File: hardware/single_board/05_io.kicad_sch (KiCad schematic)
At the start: 36 parts, among them J12 USB-C, J13 EXPANSION, J14 RS485 IN, J15 RS485 OUT, SW1 BOOTSEL, U13 USBLC6-2SC6, U14 SIT3088ETK, U15 SIT3088ETK, U17 SIT3088ETK, U18 SIT3088ETK

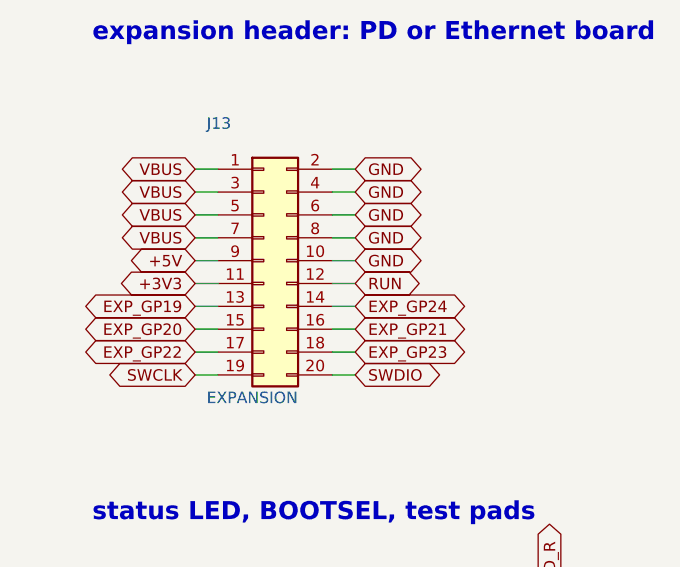
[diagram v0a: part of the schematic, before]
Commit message: Board S: screw keepouts, finer In3 centre rules, encoder on SPI0 (WIP, unrouted)
Work in progress from 2026-09-24/25, saved before routing is finished.
The board file here is the generator's output, not a routed board.

- Keepouts on F.Cu and B.Cu round the four centre motor screws
- USB-C placed tangent to the edge
- Encoder on SPI0 (ENC_DO GPIO4, ENC_SCK GPIO6); J13 pins swapped
- C901 moved north; encoder stitching vias back in the chip's pads
- "fine centre" rule area: signal nets on In3 inside R 17 may use
  0.12 mm track and clearance (servodrive_S.kicad_dru); finish.py's
  maze tries 0.12 there when 0.15 fails; the area is stripped before
  the DSN export so freerouting doesn't see it as a keepout
- Footprint tweaks: 0402 small pads, L_pol_2016, RP2350 QFN

Co-Authored-By: Claude Opus 5.5 (1M context) <noreply@anthropic.com>
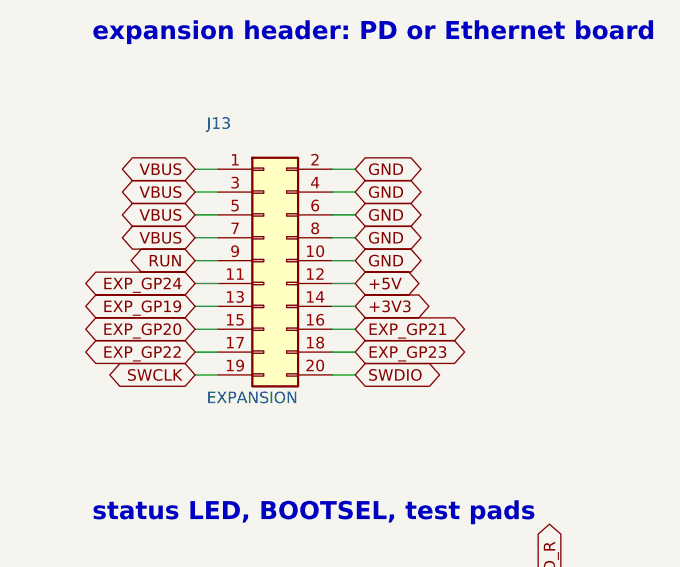
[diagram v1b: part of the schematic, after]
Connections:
- net +3V3: now also J13.14 (Pin_14); no longer J13.11 (Pin_11)
- net +5V: now also J13.12 (Pin_12); no longer J13.9 (Pin_9)
- net EXP_GP24: now also J13.11 (Pin_11); no longer J13.14 (Pin_14)
- net RUN: now also J13.9 (Pin_9); no longer J13.12 (Pin_12)
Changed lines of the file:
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@@
 	(wire (pts (xy 29.2100 220.9800) (xy 26.6700 220.9800))
 		(stroke (width 0) (type default)))
-	(global_label "+5V" (shape bidirectional)
+	(global_label "RUN" (shape bidirectional)
 		(at 26.6700 220.9800 180)
 		(effects (font (size 1.27 1.27)) (justify right))
@@
 	(wire (pts (xy 29.2100 223.5200) (xy 26.6700 223.5200))
 		(stroke (width 0) (type default)))
-	(global_label "+3V3" (shape bidirectional)
+	(global_label "EXP_GP24" (shape bidirectional)
 		(at 26.6700 223.5200 180)
 		(effects (font (size 1.27 1.27)) (justify right))
@@
 	(wire (pts (xy 41.9100 223.5200) (xy 44.4500 223.5200))
 		(stroke (width 0) (type default)))
-	(global_label "RUN" (shape bidirectional)
+	(global_label "+5V" (shape bidirectional)
 		(at 44.4500 223.5200 0)
 		(effects (font (size 1.27 1.27)) (justify left))
@@
 	(wire (pts (xy 41.9100 226.0600) (xy 44.4500 226.0600))
 		(stroke (width 0) (type default)))
-	(global_label "EXP_GP24" (shape bidirectional)
+	(global_label "+3V3" (shape bidirectional)
 		(at 44.4500 226.0600 0)
 		(effects (font (size 1.27 1.27)) (justify left))

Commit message: Board S schematic: drawn as a person would draw it
The sheets were a grid of parts with a stub and a label on every pin.
tools/schdraw.py now draws a netlist from a hand-written layout: parts
placed and turned, wires between the pins that belong together, T-joins
split with a junction dot, ground and supply symbols on power pins, labels
only where a signal leaves its block. tools/schlayout_s.py is board S's
five sheets: signal left to right, supplies up, ground down, each part's
support parts at the pin they serve, dashed frames and notes.

The drawing cannot change the circuit: every sheet is checked against
schematic_s's netlist before it is written, and `schdraw.py --check s`
compares KiCad's own netlist export net by net (it matches; ERC 0 at all
severities; PCB parity unchanged, same 219 reports as before).

Found on the way: a symbol's instance path must be /<root>/<sheet>. With
the root left out, as schematic.py writes it, KiCad joins labelled nets
but silently drops every net that is only wire.

Co-Authored-By: Claude Opus 5.5 (1M context) <noreply@anthropic.com>
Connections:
- net CC1: no longer names the net of J12.A5 (CC1), R1101.1
- net CC2: no longer names the net of J12.B5 (CC2), R1102.1
- net LED_B_K: no longer names the net of D1103.3 (BK), R1109.2
- net LED_G_K: no longer names the net of D1103.2 (GK), R1108.2
- net LED_R_K: no longer names the net of D1103.1 (RK), R1107.2
- net RS485_IN_DN_N: no longer names the net of D1101.2 (A2), J14.3 (Pin_3), R1105.2, U14.7 (B)
- net RS485_IN_DN_P: no longer names the net of D1101.1 (A1), J14.2 (Pin_2), R1105.1, U14.6 (A)
- net RS485_IN_UP_N: no longer names the net of D1102.2 (A2), J14.5 (Pin_5), U15.7 (B)
- net RS485_IN_UP_P: no longer names the net of D1102.1 (A1), J14.4 (Pin_4), U15.6 (A)
- net RS485_OUT_DN_N: no longer names the net of D1104.2 (A2), J15.3 (Pin_3), U17.7 (B)
- net RS485_OUT_DN_P: no longer names the net of D1104.1 (A1), J15.2 (Pin_2), U17.6 (A)
- net RS485_OUT_UP_N: no longer names the net of D1105.2 (A2), J15.5 (Pin_5), R1106.2, U18.7 (B)
- net RS485_OUT_UP_P: no longer names the net of D1105.1 (A1), J15.4 (Pin_4), R1106.1, U18.6 (A)
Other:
- note added: "ADC3 divider, FAULT_n pull-up"
- note added: "Expansion header: PD or Ethernet board"
- note added: "RS-485 is a CPU relay: each port is two point- to-point pairs, one in and one out, so a drive passes the chain on in software. Drivers are always enabled; each receiver has its 120R termination (R1105, R1106). R803 with the NTC (R901, sheet 01) makes FET_TEMP."
- note added: "RS-485 relay: port IN"
- note added: "RS-485 relay: port OUT"
- note added: "Status LED, BOOTSEL, test pads"
- note removed: "ADC3 front end, FAULT_n"
- note removed: "RS-485 relay"
- note removed: "expansion header: PD or Ethernet board"
- note removed: "status LED, BOOTSEL, test pads"
- moved on the sheet: C1102, C1103, C1104, C1105, C802, D1002, D1101, D1102, D1103, D1104, D1105, J12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

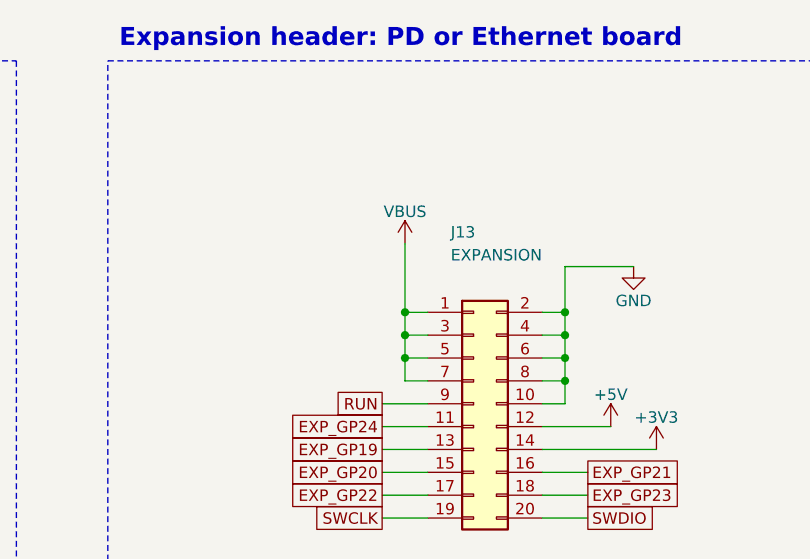
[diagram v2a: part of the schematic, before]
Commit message: Board S schematic: the header and the notes follow the netlist
J13's pins are drawn by net (VBUS row, ground row, supply pins on staggered
stubs, labels for the rest), and the encoder note reads its GPIOs off U7, so
the same layout draws main's pin map and this branch's.

Co-Authored-By: Claude Opus 5.5 (1M context) <noreply@anthropic.com>
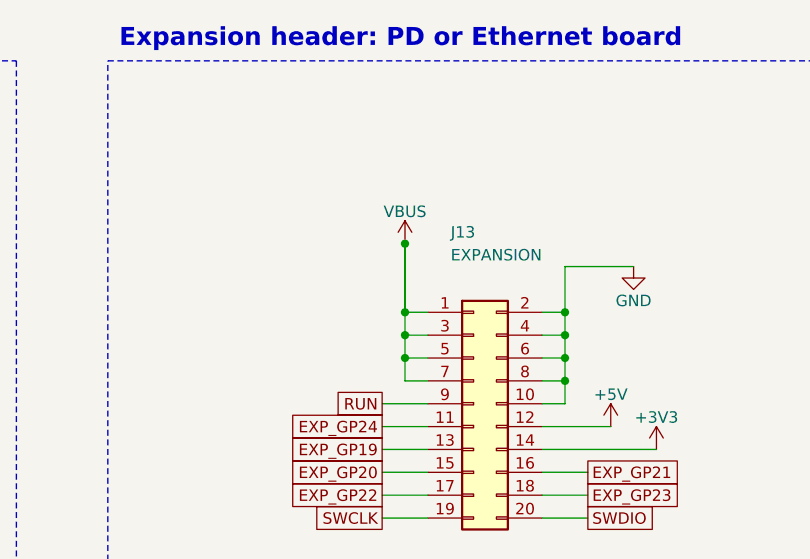
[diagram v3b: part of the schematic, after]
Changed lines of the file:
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@@
+	)
+	(symbol
+		(lib_id "power:+5V")
+		(at 236.2200 64.7700 0)
+		(unit 1)
+		(exclude_from_sim no)
+		(in_bom yes)
+		(on_board yes)
+		(dnp no)
+		(property "Reference" "#PWR6014" (at 236.2200 64.7700 0)
+			(effects (font (size 1.27 1.27)) (hide yes)))
+		(property "Value" "+5V" (at 236.2200 61.2140 0)
+			(effects (font (size 1.27 1.27))))
+		(property "Footprint" "" (at 236.2200 64.7700 0)
+			(effects (font (size 1.27 1.27)) (hide yes)))
+		(pin "1")
+		(instances (project "servodrive_S" (path "/4a000168-6f9c-5ed8-a51d-b44d8035e2cd/356eb72c-c0ed-5939-84cc-ffb56ee7ff4c" (reference "#PWR6014") (unit 1))))
+	)
+	(symbol
+		(lib_id "power:+3V3")
+		(at 241.3000 67.3100 0)
+		(unit 1)
+		(exclude_from_sim no)
+		(in_bom yes)
+		(on_board yes)
+		(dnp no)
+		(property "Reference" "#PWR6015" (at 241.3000 67.3100 0)
+			(effects (font (size 1.27 1.27)) (hide yes)))
+		(property "Value" "+3V3" (at 241.3000 63.7540 0)
+			(effects (font (size 1.27 1.27))))
+		(property "Footprint" "" (at 241.3000 67.3100 0)
+			(effects (font (size 1.27 1.27)) (hide yes)))
+		(pin "1")
+		(instances (project "servodrive_S" (path "/4a000168-6f9c-5ed8-a51d-b44d8035e2cd/356eb72c-c0ed-5939-84cc-ffb56ee7ff4c" (reference "#PWR6015") (unit 1))))
 	)
 	(symbol
@@
 		(on_board yes)
 		(dnp no)
-		(property "Reference" "#PWR6014" (at 213.3600 44.4500 0)
+		(property "Reference" "#PWR6016" (at 213.3600 44.4500 0)
 			(effects (font (size 1.27 1.27)) (hide yes)))
 		(property "Value" "VBUS" (at 213.3600 40.8940 0)
@@
 			(effects (font (size 1.27 1.27)) (hide yes)))
 		(pin "1")
-		(instances (project "servodrive_S" (path "/4a000168-6f9c-5ed8-a51d-b44d8035e2cd/356eb72c-c0ed-5939-84cc-ffb56ee7ff4c" (reference "#PWR6014") (unit 1))))
+		(instances (project "servodrive_S" (path "/4a000168-6f9c-5ed8-a51d-b44d8035e2cd/356eb72c-c0ed-5939-84cc-ffb56ee7ff4c" (reference "#PWR6016") (unit 1))))
 	)
 	(symbol
@@
 		(on_board yes)
 		(dnp no)
-		(property "Reference" "#PWR6015" (at 238.7600 46.9900 0)
+		(property "Reference" "#PWR6017" (at 238.7600 46.9900 0)
 			(effects (font (size 1.27 1.27)) (hide yes)))
 		(property "Value" "GND" (at 238.7600 50.8000 0)
 			(effects (font (size 1.27 1.27))))
 		(property "Footprint" "" (at 238.7600 46.9900 0)
-			(effects (font (size 1.27 1.27)) (hide yes)))
-		(pin "1")
-		(instances (project "servodrive_S" (path "/4a000168-6f9c-5ed8-a51d-b44d8035e2cd/356eb72c-c0ed-5939-84cc-ffb56ee7ff4c" (reference "#PWR6015") (unit 1))))
-	)
-	(symbol
-		(lib_id "power:+5V")
-		(at 236.2200 64.7700 0)
-		(unit 1)
-		(exclude_from_sim no)
-		(in_bom yes)
-		(on_board yes)
-		(dnp no)
-		(property "Reference" "#PWR6016" (at 236.2200 64.7700 0)
-			(effects (font (size 1.27 1.27)) (hide yes)))
-		(property "Value" "+5V" (at 236.2200 61.2140 0)
-			(effects (font (size 1.27 1.27))))
-		(property "Footprint" "" (at 236.2200 64.7700 0)
-			(effects (font (size 1.27 1.27)) (hide yes)))
-		(pin "1")
-		(instances (project "servodrive_S" (path "/4a000168-6f9c-5ed8-a51d-b44d8035e2cd/356eb72c-c0ed-5939-84cc-ffb56ee7ff4c" (reference "#PWR6016") (unit 1))))
-	)
-	(symbol
-		(lib_id "power:+3V3")
-		(at 241.3000 67.3100 0)
-		(unit 1)
-		(exclude_from_sim no)
-		(in_bom yes)
-		(on_board yes)
-		(dnp no)
-		(property "Reference" "#PWR6017" (at 241.3000 67.3100 0)
-			(effects (font (size 1.27 1.27)) (hide yes)))
-		(property "Value" "+3V3" (at 241.3000 63.7540 0)
-			(effects (font (size 1.27 1.27))))
-		(property "Footprint" "" (at 241.3000 67.3100 0)
 			(effects (font (size 1.27 1.27)) (hide yes)))
 		(pin "1")
@@
 	(wire (pts (xy 213.3600 52.0700) (xy 215.9000 52.0700))
 		(stroke (width 0) (type default)))
+	(wire (pts (xy 228.6000 52.0700) (xy 231.1400 52.0700))
+		(stroke (width 0) (type default)))
 	(wire (pts (xy 213.3600 54.6100) (xy 215.9000 54.6100))
 		(stroke (width 0) (type default)))
+	(wire (pts (xy 228.6000 54.6100) (xy 231.1400 54.6100))
+		(stroke (width 0) (type default)))
 	(wire (pts (xy 213.3600 57.1500) (xy 215.9000 57.1500))
 		(stroke (width 0) (type default)))
+	(wire (pts (xy 228.6000 57.1500) (xy 231.1400 57.1500))
+		(stroke (width 0) (type default)))
 	(wire (pts (xy 213.3600 59.6900) (xy 215.9000 59.6900))
 		(stroke (width 0) (type default)))
+	(wire (pts (xy 228.6000 59.6900) (xy 231.1400 59.6900))
+		(stroke (width 0) (type default)))
+	(wire (pts (xy 210.8200 62.2300) (xy 215.9000 62.2300))
+		(stroke (width 0) (type default)))
+	(wire (pts (xy 228.6000 62.2300) (xy 231.1400 62.2300))
+		(stroke (width 0) (type default)))
+	(wire (pts (xy 210.8200 64.7700) (xy 215.9000 64.7700))
+		(stroke (width 0) (type default)))
+	(wire (pts (xy 228.6000 64.7700) (xy 236.2200 64.7700))
+		(stroke (width 0) (type default)))
+	(wire (pts (xy 210.8200 67.3100) (xy 215.9000 67.3100))
+		(stroke (width 0) (type default)))
+	(wire (pts (xy 228.6000 67.3100) (xy 241.3000 67.3100))
+		(stroke (width 0) (type default)))
+	(wire (pts (xy 210.8200 69.8500) (xy 215.9000 69.8500))
+		(stroke (width 0) (type default)))
+	(wire (pts (xy 228.6000 69.8500) (xy 233.6800 69.8500))
+		(stroke (width 0) (type default)))
+	(wire (pts (xy 210.8200 72.3900) (xy 215.9000 72.3900))
+		(stroke (width 0) (type default)))
+	(wire (pts (xy 228.6000 72.3900) (xy 233.6800 72.3900))
+		(stroke (width 0) (type default)))
+	(wire (pts (xy 210.8200 74.9300) (xy 215.9000 74.9300))
+		(stroke (width 0) (type default)))
+	(wire (pts (xy 228.6000 74.9300) (xy 233.6800 74.9300))
+		(stroke (width 0) (type default)))
 	(wire (pts (xy 213.3600 44.4500) (xy 213.3600 52.0700))
 		(stroke (width 0) (type default)))
+	(wire (pts (xy 213.3600 44.4500) (xy 213.3600 52.0700))
+		(stroke (width 0) (type default)))
 	(wire (pts (xy 213.3600 52.0700) (xy 213.3600 54.6100))
 		(stroke (width 0) (type default)))
@@
 	(wire (pts (xy 213.3600 57.1500) (xy 213.3600 59.6900))
 		(stroke (width 0) (type default)))
-	(wire (pts (xy 228.6000 52.0700) (xy 231.1400 52.0700))
-		(stroke (width 0) (type default)))
-	(wire (pts (xy 228.6000 54.6100) (xy 231.1400 54.6100))
-		(stroke (width 0) (type default)))
-	(wire (pts (xy 228.6000 57.1500) (xy 231.1400 57.1500))
-		(stroke (width 0) (type default)))
-	(wire (pts (xy 228.6000 59.6900) (xy 231.1400 59.6900))
-		(stroke (width 0) (type default)))
-	(wire (pts (xy 228.6000 62.2300) (xy 231.1400 62.2300))
-		(stroke (width 0) (type default)))
 	(wire (pts (xy 231.1400 46.9900) (xy 231.1400 52.0700))
 		(stroke (width 0) (type default)))
@@
 		(stroke (width 0) (type default)))
 	(wire (pts (xy 231.1400 46.9900) (xy 238.7600 46.9900))
-		(stroke (width 0) (type default)))
-	(wire (pts (xy 228.6000 64.7700) (xy 236.2200 64.7700))
-		(stroke (width 0) (type default)))
-	(wire (pts (xy 228.6000 67.3100) (xy 241.3000 67.3100))
-		(stroke (width 0) (type default)))
-	(wire (pts (xy 210.8200 62.2300) (xy 215.9000 62.2300))
-		(stroke (width 0) (type default)))
-	(wire (pts (xy 210.8200 64.7700) (xy 215.9000 64.7700))
-		(stroke (width 0) (type default)))
-	(wire (pts (xy 210.8200 67.3100) (xy 215.9000 67.3100))
-		(stroke (width 0) (type default)))
-	(wire (pts (xy 210.8200 69.8500) (xy 215.9000 69.8500))
-		(stroke (width 0) (type default)))
-	(wire (pts (xy 210.8200 72.3900) (xy 215.9000 72.3900))
-		(stroke (width 0) (type default)))
-	(wire (pts (xy 210.8200 74.9300) (xy 215.9000 74.9300))
-		(stroke (width 0) (type default)))
-	(wire (pts (xy 228.6000 69.8500) (xy 233.6800 69.8500))
-		(stroke (width 0) (type default)))
-	(wire (pts (xy 228.6000 72.3900) (xy 233.6800 72.3900))
-		(stroke (width 0) (type default)))
-	(wire (pts (xy 228.6000 74.9300) (xy 233.6800 74.9300))
 		(stroke (width 0) (type default)))
 	(wire (pts (xy 330.2000 39.3700) (xy 345.4400 39.3700))
@@
 	(junction (at 187.9600 115.5700) (diameter 0) (color 0 0 0 0))
 	(junction (at 187.9600 166.3700) (diameter 0) (color 0 0 0 0))
+	(junction (at 213.3600 44.4500) (diameter 0) (color 0 0 0 0))
 	(junction (at 213.3600 52.0700) (diameter 0) (color 0 0 0 0))
 	(junction (at 213.3600 54.6100) (diameter 0) (color 0 0 0 0))
@@
 			(at 210.8200 69.8500 0)
 			(effects (font (size 1.27 1.27)) (hide yes))))
+	(global_label "EXP_GP21" (shape passive)
+		(at 233.6800 69.8500 0)
+		(effects (font (size 1.27 1.27)) (justify left))
+		(property "Intersheetrefs" "${INTERSHEET_REFS}"
+			(at 233.6800 69.8500 0)
+			(effects (font (size 1.27 1.27)) (hide yes))))
 	(global_label "EXP_GP22" (shape passive)
 		(at 210.8200 72.3900 180)
@@
 			(at 210.8200 72.3900 0)
 			(effects (font (size 1.27 1.27)) (hide yes))))
+	(global_label "EXP_GP23" (shape passive)
+		(at 233.6800 72.3900 0)
+		(effects (font (size 1.27 1.27)) (justify left))
+		(property "Intersheetrefs" "${INTERSHEET_REFS}"
+			(at 233.6800 72.3900 0)
+			(effects (font (size 1.27 1.27)) (hide yes))))
 	(global_label "SWCLK" (shape passive)
 		(at 210.8200 74.9300 180)
@@
 			(at 210.8200 74.9300 0)
 			(effects (font (size 1.27 1.27)) (hide yes))))
-	(global_label "EXP_GP21" (shape passive)
-		(at 233.6800 69.8500 0)
-		(effects (font (size 1.27 1.27)) (justify left))
-		(property "Intersheetrefs" "${INTERSHEET_REFS}"
-			(at 233.6800 69.8500 0)
-			(effects (font (size 1.27 1.27)) (hide yes))))
-	(global_label "EXP_GP23" (shape passive)
-		(at 233.6800 72.3900 0)
-		(effects (font (size 1.27 1.27)) (justify left))
-		(property "Intersheetrefs" "${INTERSHEET_REFS}"
-			(at 233.6800 72.3900 0)
-			(effects (font (size 1.27 1.27)) (hide yes))))
 	(global_label "SWDIO" (shape passive)
